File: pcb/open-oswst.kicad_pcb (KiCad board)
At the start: 2 copper layers, 70 x 50 mm, 16 parts

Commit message: PCB next rev: the VOL connector is the knob's I2C bus (Qwiic order)
Same JST-PH 4-pin, same place: pads GND, 3V3 (Ve), SDA (GPIO3), SCL (GPIO6),
in Qwiic order so a straight-through JST-SH to JST-PH cable fits when the
connector is on its designed side (mirrored, 3V3 and GND swap: the labels
say which is which). J3 GPIO45, the wired encoder's switch, is left free
for the SD card's CLK. Checked in KiCad: routes as expected.

Co-Authored-By: Claude Opus 5.5 <noreply@anthropic.com>
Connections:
- J3 pad GPIO3: VOL_A -> KNOB_SDA
- J3 pad GPIO45: VOL_SW -> (no net)
- J3 pad GPIO6: VOL_B -> KNOB_SCL
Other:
- board text added: "open-oswst fcaa9b2"
- board text removed: "open-oswst 4468800"
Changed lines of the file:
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@@
   (net 2 "GND")
   (net 3 "VSW")
-  (net 4 "VOL_A")
-  (net 5 "VOL_B")
-  (net 6 "VOL_SW")
+  (net 4 "Ve")
+  (net 5 "KNOB_SDA")
+  (net 6 "KNOB_SCL")
   (net 7 "PTT")
   (net 8 "SPK-")
@@
   (net 12 "BCLK")
   (net 13 "DIN")
-  (net 14 "Ve")
   (net_class "Default" ""
     (clearance 0.2)
@@
   )
   (gr_rect (start 113 113) (end 183 163) (stroke (width 0.1) (type solid)) (fill none) (layer "Edge.Cuts"))
-  (gr_text "open-oswst  4468800"
+  (gr_text "open-oswst  fcaa9b2"
     (at 148.0 161)
     (layer "F.SilkS")
@@
       (effects (font (size 1 1) (thickness 0.15)))
     )
-    (pad "A" thru_hole circle
+    (pad "GND" thru_hole circle
       (at -3.0 0)
       (size 1.5 1.5)
       (drill 0.8)
       (layers *.Cu *.Mask)
-      (net 4 "VOL_A")
-    )
-    (pad "B" thru_hole circle
-      (at -1.0 0)
-      (size 1.5 1.5)
-      (drill 0.8)
-      (layers *.Cu *.Mask)
-      (net 5 "VOL_B")
-    )
-    (pad "SW" thru_hole circle
-      (at 1.0 0)
-      (size 1.5 1.5)
-      (drill 0.8)
-      (layers *.Cu *.Mask)
-      (net 6 "VOL_SW")
-    )
-    (pad "GND" thru_hole circle
+      (net 2 "GND")
+    )
+    (pad "3V3" thru_hole circle
+      (at -1.0 0)
+      (size 1.5 1.5)
+      (drill 0.8)
+      (layers *.Cu *.Mask)
+      (net 4 "Ve")
+    )
+    (pad "SDA" thru_hole circle
+      (at 1.0 0)
+      (size 1.5 1.5)
+      (drill 0.8)
+      (layers *.Cu *.Mask)
+      (net 5 "KNOB_SDA")
+    )
+    (pad "SCL" thru_hole circle
       (at 3.0 0)
       (size 1.5 1.5)
       (drill 0.8)
       (layers *.Cu *.Mask)
-      (net 2 "GND")
+      (net 6 "KNOB_SCL")
     )
   )
@@
       (drill 1.0)
       (layers *.Cu *.Mask)
-      (net 5 "VOL_B")
+      (net 6 "KNOB_SCL")
     )
     (pad "GPIO5" thru_hole circle
@@
       (drill 1.0)
       (layers *.Cu *.Mask)
-      (net 4 "VOL_A")
+      (net 5 "KNOB_SDA")
     )
     (pad "GPIO2" thru_hole circle
@@
       (drill 1.0)
       (layers *.Cu *.Mask)
-      (net 6 "VOL_SW")
     )
     (pad "GPIO46" thru_hole circle
@@
       (drill 1.0)
       (layers *.Cu *.Mask)
-      (net 14 "Ve")
+      (net 4 "Ve")
     )
     (pad "Ve_a" thru_hole circle
@@
       (drill 1.0)
       (layers *.Cu *.Mask)
-      (net 14 "Ve")
+      (net 4 "Ve")
     )
     (pad "5V" thru_hole circle
@@
       (drill 1.0)
       (layers *.Cu *.Mask)
-      (net 14 "Ve")
+      (net 4 "Ve")
     )
     (pad "GND" thru_hole circle
@@
       (drill 1.0)
       (layers *.Cu *.Mask)
-      (net 14 "Ve")
+      (net 4 "Ve")
     )
     (pad "GND" thru_hole circle

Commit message: PCB next rev: SD card header on the top edge; BAT and SW beside HBAT/SPK
SD (#44): a 9-pin 0.1" header for the microSD breakout, soldered straight
on (in a right-angle socket), pads in the breakout's own order: 3V3 (Ve),
GND, DO (GPIO44), CMD (GPIO43), CLK (GPIO45), D3 (tied to Ve: SD mode),
D2/D1/CD unconnected. Where BAT, SW and PA were; PA is gone (no Air Buddy
since 2026-10-08). BAT and SW are a second column beside HBAT and SPK, so
the whole battery path sits in one corner. VOL and PTT don't move.

GPIO45 at boot: checked on two boards from both MAC ranges
(F8:5B:1B:A2:C8:48, 10:BD:A3:5A:60:04): VDD_SPI_FORCE is burned (3.3 V),
so a pull-up on SD CLK can't select 1.8 V flash. DRC: 0 violations.

Co-Authored-By: Claude Opus 5.5 <noreply@anthropic.com>
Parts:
- removed PA: , JST_PH_B2B
- added SD: , PinHeader_1x9_P2.54mm, F.Cu at (136.0, 117.0)
- moved SW 14.3 mm to (125.0, 129.5), turned to 90 degrees
- moved BAT 5.50 mm to (125.0, 122.5), turned to 90 degrees
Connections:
- J2 pad GPIO43: (no net) -> SD_CMD
- J2 pad GPIO44: (no net) -> SD_D0
- J3 pad GPIO45: (no net) -> SD_CLK
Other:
- board text added: "open-oswst cf52971"
- board text removed: "open-oswst fcaa9b2"
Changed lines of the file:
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@@
   )
   (net 0 "")
-  (net 1 "VBAT")
+  (net 1 "Ve")
   (net 2 "GND")
-  (net 3 "VSW")
-  (net 4 "Ve")
-  (net 5 "KNOB_SDA")
-  (net 6 "KNOB_SCL")
-  (net 7 "PTT")
-  (net 8 "SPK-")
-  (net 9 "SPK+")
-  (net 10 "MIC_OUT")
-  (net 11 "LRC")
-  (net 12 "BCLK")
-  (net 13 "DIN")
+  (net 3 "SD_D0")
+  (net 4 "SD_CMD")
+  (net 5 "SD_CLK")
+  (net 6 "KNOB_SDA")
+  (net 7 "KNOB_SCL")
+  (net 8 "PTT")
+  (net 9 "VBAT")
+  (net 10 "VSW")
+  (net 11 "SPK-")
+  (net 12 "SPK+")
+  (net 13 "MIC_OUT")
+  (net 14 "LRC")
+  (net 15 "BCLK")
+  (net 16 "DIN")
   (net_class "Default" ""
     (clearance 0.2)
@@
   )
   (gr_rect (start 113 113) (end 183 163) (stroke (width 0.1) (type solid)) (fill none) (layer "Edge.Cuts"))
-  (gr_text "open-oswst  fcaa9b2"
+  (gr_text "open-oswst  cf52971"
     (at 148.0 161)
     (layer "F.SilkS")
@@
     )
   )
+  (footprint "PinHeader_1x9_P2.54mm"
+    (layer "F.Cu")
+    (at 136 117)
+    (fp_text reference "SD" (at 0 -2.5) (layer "F.SilkS")
+      (effects (font (size 1 1) (thickness 0.15)))
+    )
+    (pad "3V3" thru_hole circle
+      (at -10.16 0)
+      (size 1.7 1.7)
+      (drill 1.0)
+      (layers *.Cu *.Mask)
+      (net 1 "Ve")
+    )
+    (pad "GND" thru_hole circle
+      (at -7.62 0)
+      (size 1.7 1.7)
+      (drill 1.0)
+      (layers *.Cu *.Mask)
+      (net 2 "GND")
+    )
+    (pad "DO" thru_hole circle
+      (at -5.08 0)
+      (size 1.7 1.7)
+      (drill 1.0)
+      (layers *.Cu *.Mask)
+      (net 3 "SD_D0")
+    )
+    (pad "CMD" thru_hole circle
+      (at -2.54 0)
+      (size 1.7 1.7)
+      (drill 1.0)
+      (layers *.Cu *.Mask)
+      (net 4 "SD_CMD")
+    )
+    (pad "CLK" thru_hole circle
+      (at 0.0 0)
+      (size 1.7 1.7)
+      (drill 1.0)
+      (layers *.Cu *.Mask)
+      (net 5 "SD_CLK")
+    )
+    (pad "D3" thru_hole circle
+      (at 2.539999999999999 0)
+      (size 1.7 1.7)
+      (drill 1.0)
+      (layers *.Cu *.Mask)
+      (net 1 "Ve")
+    )
+    (pad "D2" thru_hole circle
+      (at 5.08 0)
+      (size 1.7 1.7)
+      (drill 1.0)
+      (layers *.Cu *.Mask)
+    )
+    (pad "D1" thru_hole circle
+      (at 7.620000000000001 0)
+      (size 1.7 1.7)
+      (drill 1.0)
+      (layers *.Cu *.Mask)
+    )
+    (pad "CD" thru_hole circle
+      (at 10.16 0)
+      (size 1.7 1.7)
+      (drill 1.0)
+      (layers *.Cu *.Mask)
+    )
+  )
+  (footprint "JST_PH_B4B"
+    (layer "F.Cu")
+    (at 160 117)
+    (fp_text reference "VOL" (at 0 -2.5) (layer "F.SilkS")
+      (effects (font (size 1 1) (thickness 0.15)))
+    )
+    (pad "GND" thru_hole circle
+      (at -3.0 0)
+      (size 1.5 1.5)
+      (drill 0.8)
+      (layers *.Cu *.Mask)
+      (net 2 "GND")
+    )
+    (pad "3V3" thru_hole circle
+      (at -1.0 0)
+      (size 1.5 1.5)
+      (drill 0.8)
+      (layers *.Cu *.Mask)
+      (net 1 "Ve")
+    )
+    (pad "SDA" thru_hole circle
+      (at 1.0 0)
+      (size 1.5 1.5)
+      (drill 0.8)
+      (layers *.Cu *.Mask)
+      (net 6 "KNOB_SDA")
+    )
+    (pad "SCL" thru_hole circle
+      (at 3.0 0)
+      (size 1.5 1.5)
+      (drill 0.8)
+      (layers *.Cu *.Mask)
+      (net 7 "KNOB_SCL")
+    )
+  )
   (footprint "JST_PH_B2B"
     (layer "F.Cu")
-    (at 125 117)
+    (at 170 117)
+    (fp_text reference "PTT" (at 0 -2.5) (layer "F.SilkS")
+      (effects (font (size 1 1) (thickness 0.15)))
+    )
+    (pad "1" thru_hole circle
+      (at -1.0 0)
+      (size 1.5 1.5)
+      (drill 0.8)
+      (layers *.Cu *.Mask)
+      (net 8 "PTT")
+    )
+    (pad "2" thru_hole circle
+      (at 1.0 0)
+      (size 1.5 1.5)
+      (drill 0.8)
+      (layers *.Cu *.Mask)
+      (net 2 "GND")
+    )
+  )
+  (footprint "JST_PH_B2B"
+    (layer "F.Cu")
+    (at 125 122.5 90)
     (fp_text reference "BAT" (at 0 -2.5) (layer "F.SilkS")
       (effects (font (size 1 1) (thickness 0.15)))
@@
       (drill 0.8)
       (layers *.Cu *.Mask)
-      (net 1 "VBAT")
+      (net 9 "VBAT")
     )
     (pad "-" thru_hole circle
@@
   (footprint "JST_PH_B2B"
     (layer "F.Cu")
-    (at 132 117)
+    (at 125 129.5 90)
     (fp_text reference "SW" (at 0 -2.5) (layer "F.SilkS")
       (effects (font (size 1 1) (thickness 0.15)))
@@
       (drill 0.8)
       (layers *.Cu *.Mask)
-      (net 1 "VBAT")
+      (net 9 "VBAT")
     )
     (pad "2" thru_hole circle
@@
       (drill 0.8)
       (layers *.Cu *.Mask)
-      (net 3 "VSW")
+      (net 10 "VSW")
     )
   )
   (footprint "JST_PH_B2B"
     (layer "F.Cu")
-    (at 139 117)
-    (fp_text reference "PA" (at 0 -2.5) (layer "F.SilkS")
+    (at 118 122.5 90)
+    (fp_text reference "HBAT" (at 0 -2.5) (layer "F.SilkS")
       (effects (font (size 1 1) (thickness 0.15)))
     )
@@
       (drill 0.8)
       (layers *.Cu *.Mask)
-      (net 3 "VSW")
+      (net 10 "VSW")
     )
     (pad "-" thru_hole circle
@@
     )
   )
-  (footprint "JST_PH_B4B"
-    (layer "F.Cu")
-    (at 160 117)
-    (fp_text reference "VOL" (at 0 -2.5) (layer "F.SilkS")
-      (effects (font (size 1 1) (thickness 0.15)))
-    )
-    (pad "GND" thru_hole circle
-      (at -3.0 0)
-      (size 1.5 1.5)
-      (drill 0.8)
-      (layers *.Cu *.Mask)
-      (net 2 "GND")
-    )
-    (pad "3V3" thru_hole circle
-      (at -1.0 0)
-      (size 1.5 1.5)
-      (drill 0.8)
-      (layers *.Cu *.Mask)
-      (net 4 "Ve")
-    )
-    (pad "SDA" thru_hole circle
-      (at 1.0 0)
-      (size 1.5 1.5)
-      (drill 0.8)
-      (layers *.Cu *.Mask)
-      (net 5 "KNOB_SDA")
-    )
-    (pad "SCL" thru_hole circle
-      (at 3.0 0)
-      (size 1.5 1.5)
-      (drill 0.8)
-      (layers *.Cu *.Mask)
-      (net 6 "KNOB_SCL")
-    )
-  )
-  (footprint "JST_PH_B2B"
-    (layer "F.Cu")
-    (at 170 117)
-    (fp_text reference "PTT" (at 0 -2.5) (layer "F.SilkS")
-      (effects (font (size 1 1) (thickness 0.15)))
-    )
-    (pad "1" thru_hole circle
-      (at -1.0 0)
-      (size 1.5 1.5)
-      (drill 0.8)
-      (layers *.Cu *.Mask)
-      (net 7 "PTT")
-    )
-    (pad "2" thru_hole circle
-      (at 1.0 0)
-      (size 1.5 1.5)
-      (drill 0.8)
-      (layers *.Cu *.Mask)
-      (net 2 "GND")
-    )
-  )
-  (footprint "JST_PH_B2B"
-    (layer "F.Cu")
-    (at 118 122.5 90)
-    (fp_text reference "HBAT" (at 0 -2.5) (layer "F.SilkS")
-      (effects (font (size 1 1) (thickness 0.15)))
-    )
-    (pad "+" thru_hole circle
-      (at -1.0 0)
-      (size 1.5 1.5)
-      (drill 0.8)
-      (layers *.Cu *.Mask)
-      (net 3 "VSW")
-    )
-    (pad "-" thru_hole circle
-      (at 1.0 0)
-      (size 1.5 1.5)
-      (drill 0.8)
-      (layers *.Cu *.Mask)
-      (net 2 "GND")
-    )
-  )
   (footprint "JST_PH_B2B"
     (layer "F.Cu")
@@
       (drill 0.8)
       (layers *.Cu *.Mask)
-      (net 8 "SPK-")
+      (net 11 "SPK-")
     )
     (pad "+" thru_hole circle
@@
       (drill 0.8)
       (layers *.Cu *.Mask)
-      (net 9 "SPK+")
+      (net 12 "SPK+")
     )
   )
@@
       (drill 1.0)
       (layers *.Cu *.Mask)
-      (net 6 "KNOB_SCL")
+      (net 7 "KNOB_SCL")
     )
     (pad "GPIO5" thru_hole circle
@@
       (drill 1.0)
       (layers *.Cu *.Mask)
-      (net 10 "MIC_OUT")
+      (net 13 "MIC_OUT")
     )
     (pad "GPIO3" thru_hole circle
@@
       (drill 1.0)
       (layers *.Cu *.Mask)
-      (net 5 "KNOB_SDA")
+      (net 6 "KNOB_SDA")
     )
     (pad "GPIO2" thru_hole circle
@@
       (drill 1.0)
       (layers *.Cu *.Mask)
+      (net 5 "SD_CLK")
     )
     (pad "GPIO46" thru_hole circle
@@
       (drill 1.0)
       (layers *.Cu *.Mask)
-      (net 11 "LRC")
+      (net 14 "LRC")
     )
     (pad "GPIO47" thru_hole circle
@@
       (drill 1.0)
       (layers *.Cu *.Mask)
-      (net 12 "BCLK")
+      (net 15 "BCLK")
     )
     (pad "GPIO33" thru_hole circle
@@
       (drill 1.0)
       (layers *.Cu *.Mask)
-      (net 13 "DIN")
+      (net 16 "DIN")
     )
     (pad "GPIO34" thru_hole circle
@@
       (drill 1.0)
       (layers *.Cu *.Mask)
-      (net 7 "PTT")
+      (net 8 "PTT")
     )
     (pad "RST" thru_hole circle
@@
       (drill 1.0)
       (layers *.Cu *.Mask)
+      (net 4 "SD_CMD")
     )
     (pad "GPIO44" thru_hole circle
@@
       (drill 1.0)
       (layers *.Cu *.Mask)
+      (net 3 "SD_D0")
     )
     (pad "Ve_b" thru_hole circle
@@
       (drill 1.0)
       (layers *.Cu *.Mask)
-      (net 4 "Ve")
+      (net 1 "Ve")
     )
     (pad "Ve_a" thru_hole circle
@@
       (drill 1.0)
       (layers *.Cu *.Mask)
-      (net 4 "Ve")
+      (net 1 "Ve")
     )
     (pad "5V" thru_hole circle
@@
       (drill 1.0)
       (layers *.Cu *.Mask)
-      (net 10 "MIC_OUT")
+      (net 13 "MIC_OUT")
     )
     (pad "GAIN" thru_hole circle
@@
       (drill 1.0)
       (layers *.Cu *.Mask)
-      (net 4 "Ve")
+      (net 1 "Ve")
     )
     (pad "GND" thru_hole circle
@@
       (drill 1.0)
       (layers *.Cu *.Mask)
-      (net 4 "Ve")
+      (net 1 "Ve")
     )
     (pad "GND" thru_hole circle
@@
       (drill 1.0)
       (layers *.Cu *.Mask)
-      (net 13 "DIN")
+      (net 16 "DIN")
     )
     (pad "BCLK" thru_hole circle
@@
       (drill 1.0)
       (layers *.Cu *.Mask)
-      (net 12 "BCLK")
+      (net 15 "BCLK")
     )
     (pad "LRC" thru_hole circle
@@
       (drill 1.0)
       (layers *.Cu *.Mask)
-      (net 11 "LRC")
+      (net 14 "LRC")
     )
   )
@@
       (drill 1.0)
       (layers *.Cu *.Mask)
-      (net 9 "SPK+")
+      (net 12 "SPK+")
     )
     (pad "-" thru_hole circle
@@
       (drill 1.0)
       (layers *.Cu *.Mask)
-      (net 8 "SPK-")
-    )
-  )
+      (net 11 "SPK-")
+    )
+  )

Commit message: PCB: make.py does route, fill, DRC, Gerbers and drill in one go; GND stitching vias
pcb/make.py replaces the clicking: board.py generates the board, freerouting
routes it headless (Specctra out and back through KiCad's pcbnew module),
every zone is filled, kicad-cli runs DRC on the routed board (any violation,
warnings and unconnected items included, stops it), then plots the seven
Gerber layers (Edge.Cuts included) and both drill files into pcb/out/fab/,
checks them, and zips them for JLCPCB. Freerouting runs with its analytics
off. Intermediates in pcb/out/route/; pcb/out stays ignored.

kicad.py: add_via. board.py: 8 GND stitching vias across the open middle,
under the Heltec: the routed board had a ~20x25 mm hole in the F.Cu ground
there (an island, dropped), under the SD lines that will run 20-40 MHz.

First run: 73 tracks and vias, DRC 0 violations / 0 unconnected, 10 files,
81 plated holes (73 pads + 8 vias), 4 unplated.

Co-Authored-By: Claude Opus 5.5 <noreply@anthropic.com>
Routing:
- net GND: vias 0 -> 8
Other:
- board text added: "open-oswst f92e84b"
- board text removed: "open-oswst cf52971"
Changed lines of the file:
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@@
   )
   (gr_rect (start 113 113) (end 183 163) (stroke (width 0.1) (type solid)) (fill none) (layer "Edge.Cuts"))
-  (gr_text "open-oswst  cf52971"
+  (gr_text "open-oswst  f92e84b"
     (at 148.0 161)
     (layer "F.SilkS")
@@
     )
   )
+  (via (at 150 129.57) (size 0.6) (drill 0.3) (layers "F.Cu" "B.Cu") (net 2))
+  (via (at 150 137.57) (size 0.6) (drill 0.3) (layers "F.Cu" "B.Cu") (net 2))
+  (via (at 158 129.57) (size 0.6) (drill 0.3) (layers "F.Cu" "B.Cu") (net 2))
+  (via (at 158 137.57) (size 0.6) (drill 0.3) (layers "F.Cu" "B.Cu") (net 2))
+  (via (at 166 129.57) (size 0.6) (drill 0.3) (layers "F.Cu" "B.Cu") (net 2))
+  (via (at 166 137.57) (size 0.6) (drill 0.3) (layers "F.Cu" "B.Cu") (net 2))
+  (via (at 174 129.57) (size 0.6) (drill 0.3) (layers "F.Cu" "B.Cu") (net 2))
+  (via (at 174 137.57) (size 0.6) (drill 0.3) (layers "F.Cu" "B.Cu") (net 2))
   (zone
     (net 2)
@@
       (thermal_gap 0.3)
       (thermal_bridge_width 0.3)
-      (island_removal_mode 2)
+      (island_removal_mode 0)
       (island_area_min 10)
     )

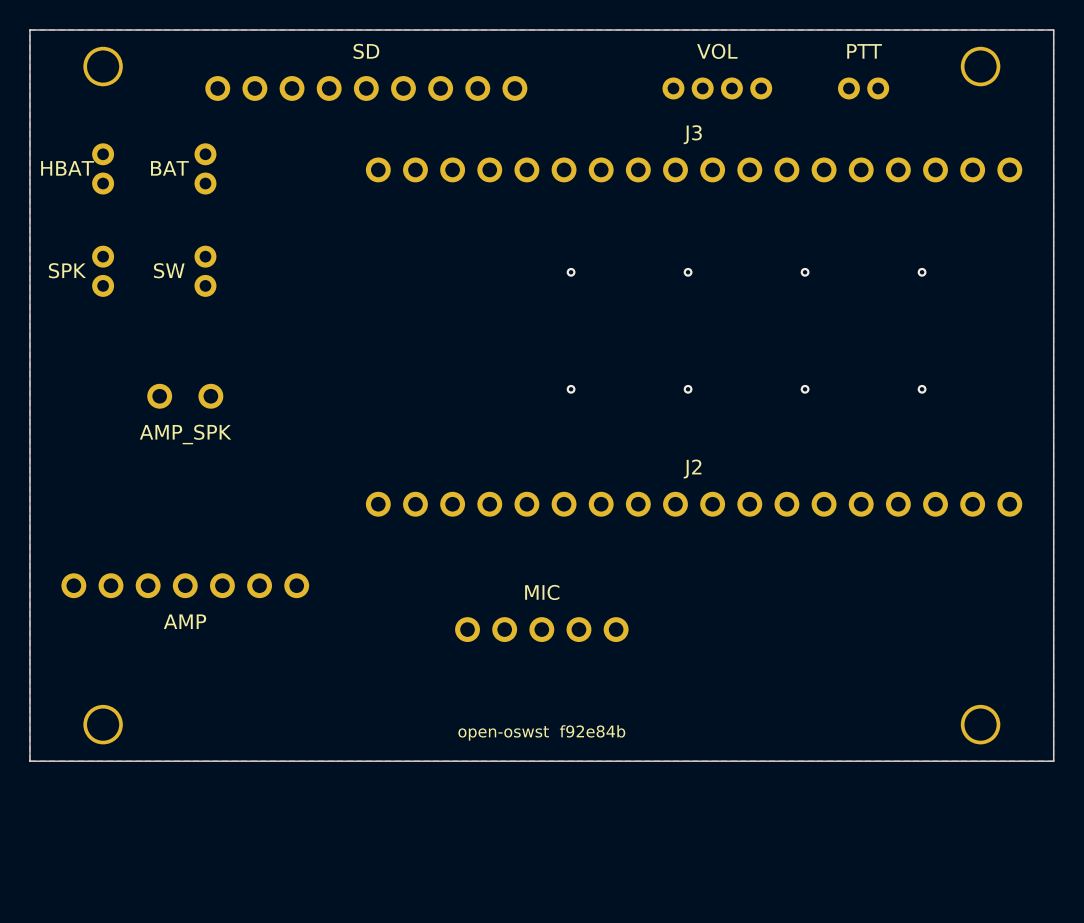
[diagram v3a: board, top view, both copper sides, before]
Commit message: Rev 10 PCB: 9 mm longer, Kenwood K1 jacks on board, connectors regrouped
The board grows 9 mm at the bottom edge (70 x 59), 1.4 mm clear of the
case's bottom lid posts; the bottom mounting holes follow it, and so do
the case's posts. REV = 10.

The K1 jacks from the homemade breakout go in the top left: the same
measured footprints (pcb/k1/k1_jacks.json) and 10-pin header map, bores
out the left edge, mirrored (the jacks mount from the back). Their nets
touch nothing else. Header ends and jack sizes are labelled on both
silkscreens; back-side text is now mirrored so it reads from the back.

To clear the top left: the amp moves down by the bottom-left hole, SPK
beside it, BAT/HBAT join SW and PTT on the top edge (BAT -> SW -> HBAT
side by side, so the 0.5 mm power traces never cross the Heltec's header
rows), SD one pin left, VOL to the right edge. The Heltec moves 3 mm down
for the top-edge traces; the case's screen window and USB-C hole follow.
Routes with freerouting: 0 unrouted, DRC clean.

Co-Authored-By: Claude Opus 5.5 <noreply@anthropic.com>
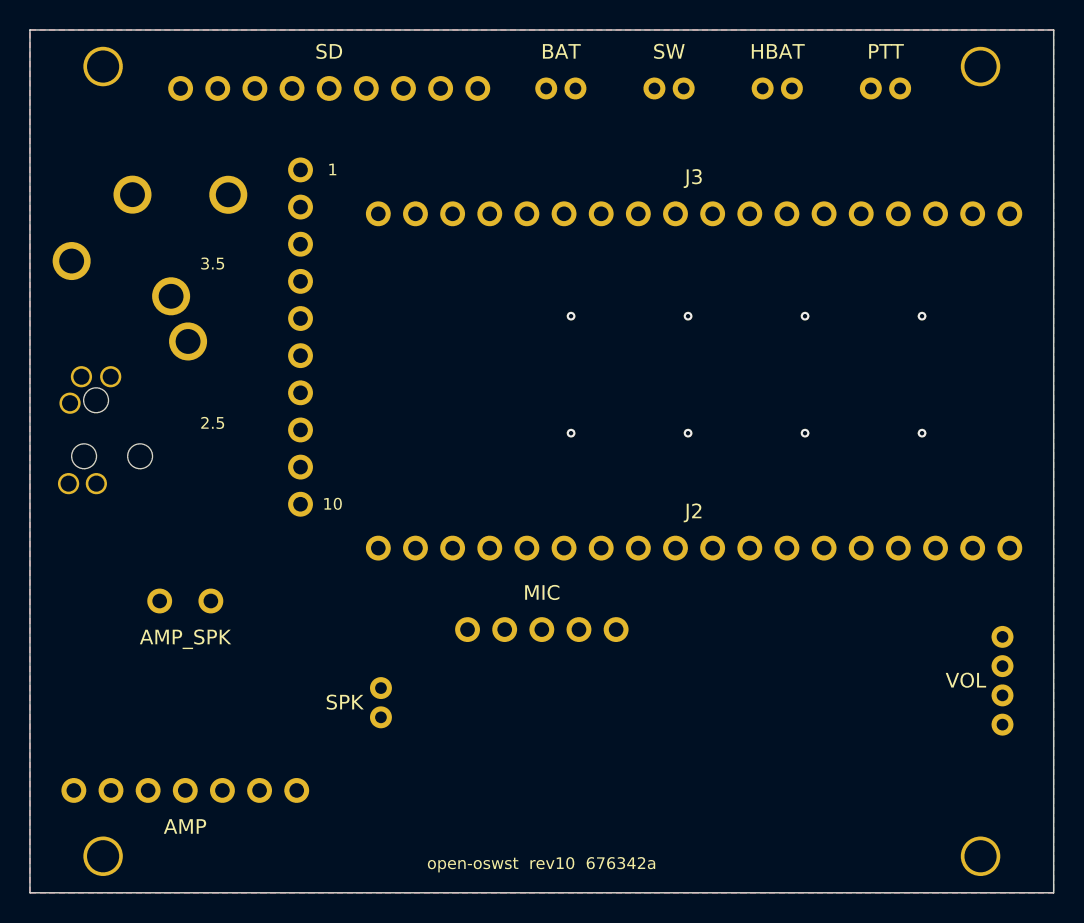
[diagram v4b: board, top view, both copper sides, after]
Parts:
- added K1: , PinHeader_1x10_P2.54mm, F.Cu at (0.00, 0.00)
- added K1_2.5: , K1_Jack_2.5mm_measured, F.Cu at (0.00, 0.00)
- added K1_3.5: , K1_Jack_3.5mm_measured, F.Cu at (0.00, 0.00)
- moved HBAT 46.4 mm to (164.1, 117.0), turned to 0 degrees
- moved VOL 44.9 mm to (179.5, 157.5), turned to 90 degrees
- moved SPK 35.1 mm to (137.0, 159.0)
- moved SW 34.1 mm to (156.7, 117.0), turned to 0 degrees
- moved BAT 24.9 mm to (149.3, 117.0), turned to 0 degrees
- moved AMP 14.0 mm to (123.6, 165.0)
- moved AMP_SPK 14.0 mm to (123.6, 152.0)
- moved H2 9.00 mm to (118.0, 169.5)
- moved H4 9.00 mm to (178.0, 169.5)
- moved J2 3.00 mm to (158.4, 148.4)
- moved J3 3.00 mm to (158.4, 125.6)
- moved SD 2.54 mm to (133.5, 117.0)
- moved PTT 1.50 mm to (171.5, 117.0)
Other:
- board size 70 x 50 mm -> 70 x 59 mm
- board text added: "1"
- board text added: "10"
- board text added: "2.5"
- board text added: "3.5"
- board text added: "open-oswst rev10 676342a"
- board text removed: "open-oswst f92e84b"
